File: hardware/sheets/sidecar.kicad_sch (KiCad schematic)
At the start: 6 parts, among them J1 ISA 8-bit (60p)

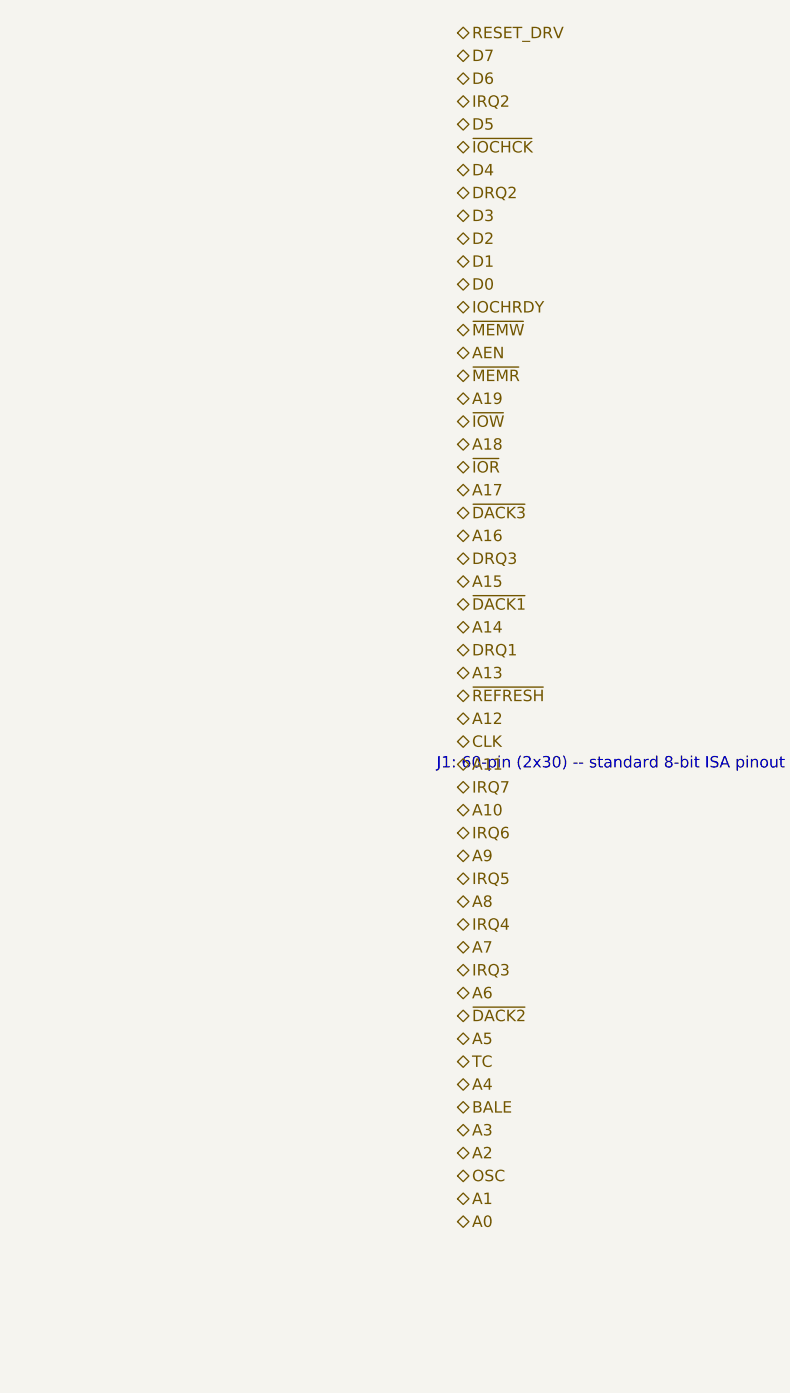
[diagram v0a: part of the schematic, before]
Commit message: ERC cleanup: NC flags on unused pins, anchored interface labels
KiCad 10 ERC drops from 366 to 16 violations, all noise:

- NC flags on the 36 genuinely unused pins (cpu_core '138/'161 spares,
  Supervisor RP2040 unused GPIO, Core2350B GPIO44-47, rtc '138 spares).
- emit_interface anchors every hier label on a stub wire ending in a
  same-name local label -- connectivity unchanged (still by name;
  netlist spans verified), but nothing dangles.
- Interface honesty: cpu_core drops AEN/IOCHRDY from PINS (both live on
  bus_mcu; nothing here touched them), bus_mcu drops PRIV_COUNTER (the
  counter chain is on-sheet, CNT_* never crosses).
- Remaining 6 label_dangling are root IRQ9-13/15: single-sheet by
  design (soft-PIC pull-ups await future 16-bit sources); kept in PINS
  as the AT-style contract.

Co-Authored-By: Claude Fable 5 <noreply@anthropic.com>
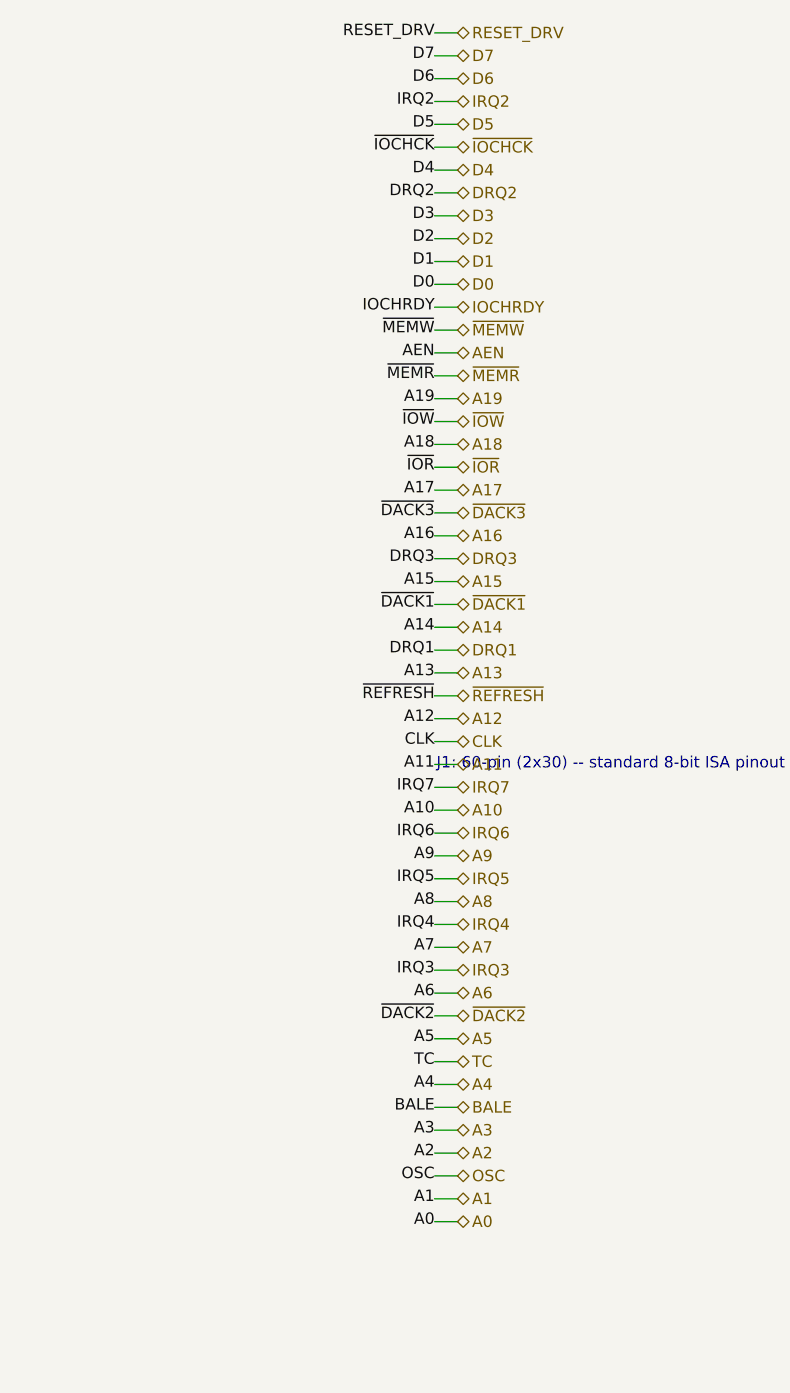
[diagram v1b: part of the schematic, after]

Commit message: Parts: footprints for all components, close 6 LCSC map gaps, check_parts.py
- mxsch.py emits the Footprint property from component props (was
  hard-coded empty); parts.py entries now carry a verified KiCad
  footprint, applied at build time alongside the LCSC number.
- Map keys fixed to match placed values: USB_PROG, SS34, LED (PicoGUS),
  APS6404L, CB3T3257/45 -- every combo across all sheets + cards now
  resolves (130 combos, 455 netlist components, all with footprints).
- Package corrections from JLC DB re-check: RTL8019AS is QFP-100 14x20
  P0.65 (not TQFP); C2897411 female header is a 2x10 strip -- fine for
  Core2350B, Pico needs 2x 1x20 (noted in jlcpcb-sourcing.md).
- 10 mini-xt:* placeholder footprints mark parts whose land pattern is
  authored at layout from the EasyEDA data (CH224K, magnetics, RJ45,
  HDMI, CF socket, ISA slot, switches, Core2350B PGA).
- New tools/check_parts.py: fails on unmapped combos, missing fp
  fields, or footprints absent from the installed KiCad libs.

Co-Authored-By: Claude Fable 5 <noreply@anthropic.com>
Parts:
- C1, C2: footprint (none) -> Capacitor_SMD:C_0603_1608Metric
- C3: footprint (none) -> Capacitor_SMD:C_1206_3216Metric
- D1: footprint (none) -> Diode_SMD:D_SMB
- F1: footprint (none) -> Fuse:Fuse_1812_4532Metric
- J1: footprint (none) -> Connector_PinHeader_2.54mm:PinHeader_2x30_P2.54mm_Vertical
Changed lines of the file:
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@@
 			)
 		)
-		(property "Footprint" ""
+		(property "Footprint" "Connector_PinHeader_2.54mm:PinHeader_2x30_P2.54mm_Vertical"
 			(at 177.8 152.4 0)
 			(effects
@@
 			)
 		)
-		(property "Footprint" ""
+		(property "Footprint" "Fuse:Fuse_1812_4532Metric"
 			(at 203.2 109.22 0)
 			(effects
@@
 			)
 		)
-		(property "Footprint" ""
+		(property "Footprint" "Diode_SMD:D_SMB"
 			(at 218.44 109.22 0)
 			(effects
@@
 			)
 		)
-		(property "Footprint" ""
+		(property "Footprint" "Capacitor_SMD:C_1206_3216Metric"
 			(at 231.14 134.62 0)
 			(effects
@@
 			)
 		)
-		(property "Footprint" ""
+		(property "Footprint" "Capacitor_SMD:C_0603_1608Metric"
 			(at 205.74 134.62 0)
 			(effects
@@
 			)
 		)
-		(property "Footprint" ""
+		(property "Footprint" "Capacitor_SMD:C_0603_1608Metric"
 			(at 218.44 134.62 0)
 			(effects

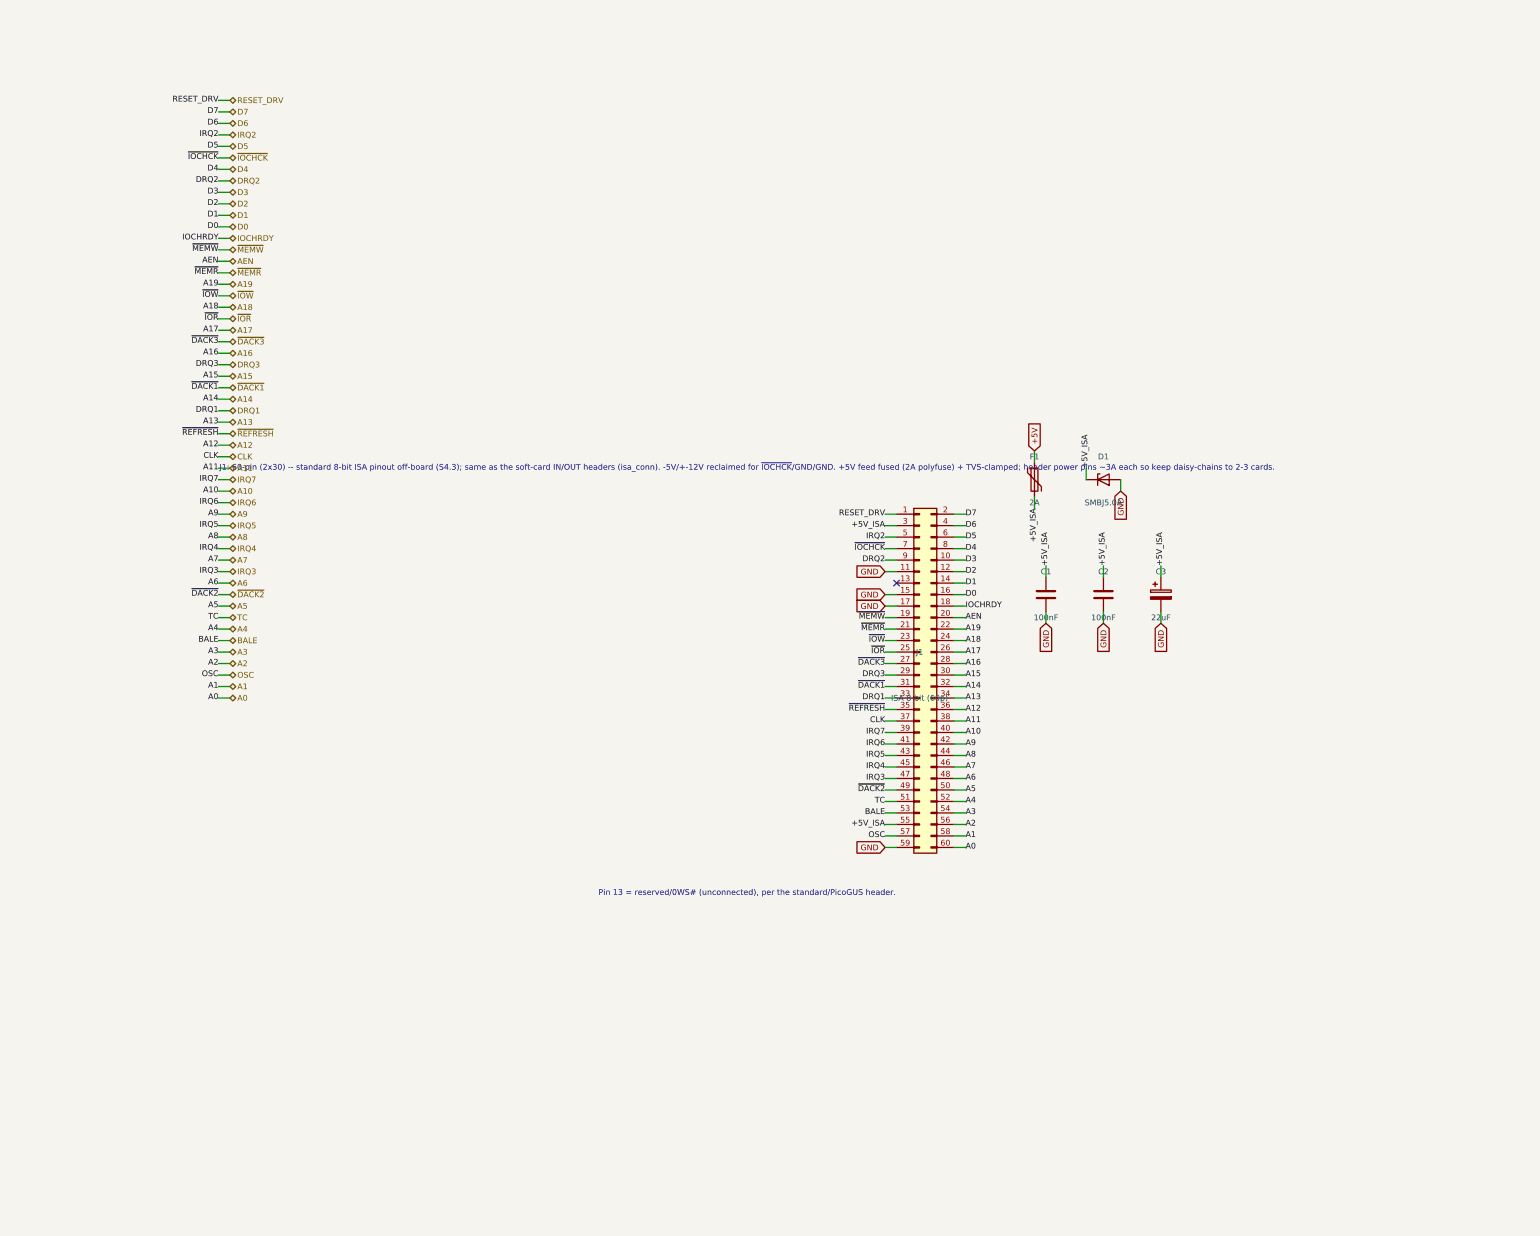
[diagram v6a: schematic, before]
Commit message: sidecar: isolation/buffer bank -- 5V-compatible ISA expansion port
Rewrite the sidecar from a passive 60-pin pass-through into the 3.3V board's
only real-ISA attachment point: an LVC buffer bank (5V-tolerant inputs,
3.3V-TTL outputs) between the internal bus and an external ISA header whose
bus-side nets are port-local (X_*, via isa_conn remap).

- Outbound: 3x 74LVC245A (A0-19 + BALE/AEN/CLK/OSC, DIR strapped outbound) +
  2x 74LVC244A (MEMR/MEMW/IOR/IOW, RESET_DRV, TC, DACK1-3, REFRESH).
- Data: 1x 74LVC245A, DIR = EXP_DDIR, R1 pulls it outbound-safe at power-on
  (DIR=H => A->B; truth table in comment). ~OE tied enabled.
- Inbound: X_IRQ2-7/X_DRQ1-3 -> EXT_* via 2x 74LVC244A, 100k pull-downs on
  every X_ input (unplugged reads all-zeros).
- IOCHRDY/~{IOCHCK}: 74LVC2G07 open-drain (2G06 body + value override) drives
  the internal nets, 10k pull-ups on the X_ side (wired-AND, no contention).
- PINS: filtered copy of isa_conn.ISA_PINS (IRQ/DRQ dropped -> EXT_*), plus
  PRIV_EXP (EXP_DDIR in, EXT_* out); IOCHRDY/~{IOCHCK} kept.

Also refreshes stale build outputs from earlier 3v3 tasks that had edited
sources without rebuilding (network/picogus sheets, card_video net renames),
so committed outputs match current sources. validate_sheet sidecar: zero
structural; build.py exit 0.

Co-Authored-By: Claude Fable 5 <noreply@anthropic.com>
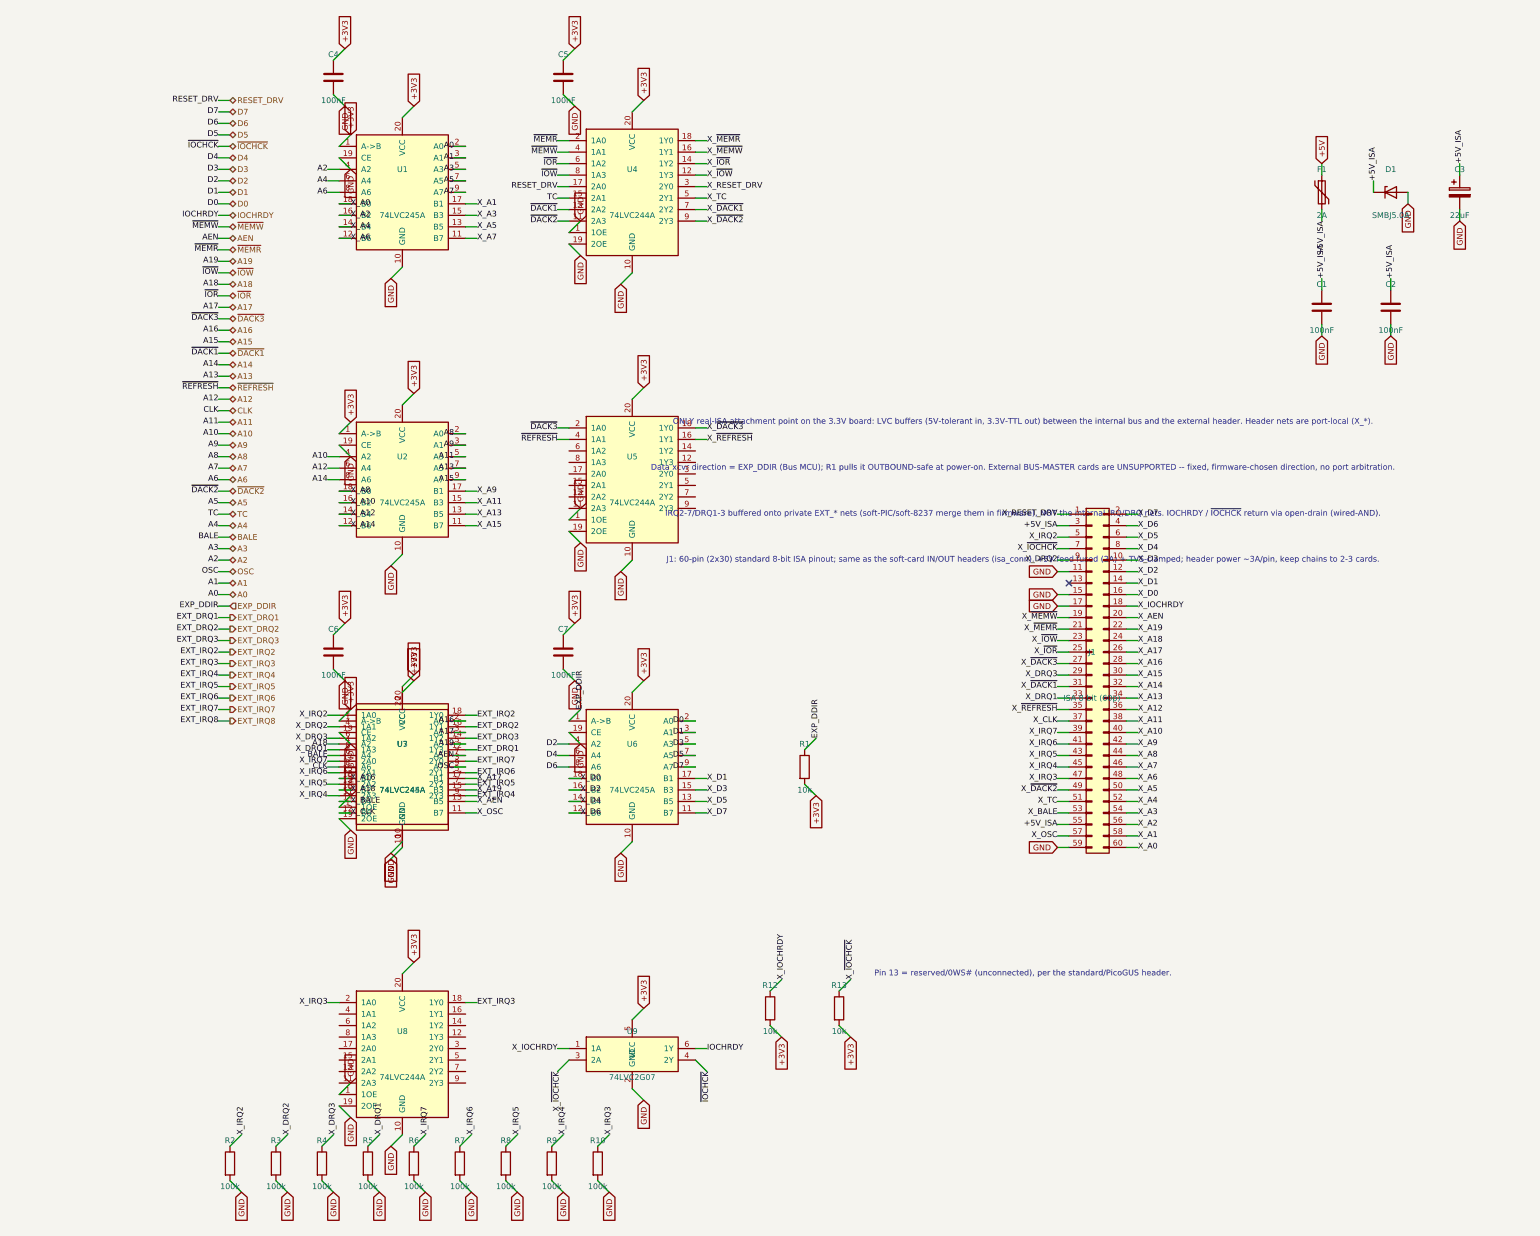
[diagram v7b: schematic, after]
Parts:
- added C4, C5, C6, C7: 100nF, Capacitor_SMD:C_0603_1608Metric, symbol Device:C
- added R1, R12, R13: 10k, Resistor_SMD:R_0603_1608Metric, symbol Device:R
- added R10, R2, R3, R4, R5, R6, R7, R8, R9: 100k, Resistor_SMD:R_0603_1608Metric, symbol Device:R
- added U1, U2, U3, U6: 74LVC245A, Package_SO:TSSOP-20_4.4x6.5mm_P0.65mm, symbol mini-xt:74HCT245
- added U4, U5, U7, U8: 74LVC244A, Package_SO:TSSOP-20_4.4x6.5mm_P0.65mm, symbol mini-xt:74HCT244
- added U9: 74LVC2G07, Package_TO_SOT_SMD:SOT-23-6, symbol mini-xt:74LVC2G06
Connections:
- net A0: now also U1.2 (A0); no longer J1.60 (Pin_60)
- net A1: now also U1.3 (A1); no longer J1.58 (Pin_58)
- net A10: now also U2.4 (A2); no longer J1.40 (Pin_40)
- net A11: now also U2.5 (A3); no longer J1.38 (Pin_38)
- net A12: now also U2.6 (A4); no longer J1.36 (Pin_36)
- net A13: now also U2.7 (A5); no longer J1.34 (Pin_34)
- net A14: now also U2.8 (A6); no longer J1.32 (Pin_32)
- net A15: now also U2.9 (A7); no longer J1.30 (Pin_30)
- net A16: now also U3.2 (A0); no longer J1.28 (Pin_28)
- net A17: now also U3.3 (A1); no longer J1.26 (Pin_26)
- net A18: now also U3.4 (A2); no longer J1.24 (Pin_24)
- net A19: now also U3.5 (A3); no longer J1.22 (Pin_22)
- net A2: now also U1.4 (A2); no longer J1.56 (Pin_56)
- net A3: now also U1.5 (A3); no longer J1.54 (Pin_54)
- net A4: now also U1.6 (A4); no longer J1.52 (Pin_52)
- net A5: now also U1.7 (A5); no longer J1.50 (Pin_50)
- net A6: now also U1.8 (A6); no longer J1.48 (Pin_48)
- net A7: now also U1.9 (A7); no longer J1.46 (Pin_46)
- net A8: now also U2.2 (A0); no longer J1.44 (Pin_44)
- net A9: now also U2.3 (A1); no longer J1.42 (Pin_42)
- net AEN: now also U3.7 (A5); no longer J1.20 (Pin_20)
- net BALE: now also U3.6 (A4); no longer J1.53 (Pin_53)
- net CLK: now also U3.8 (A6); no longer J1.37 (Pin_37)
- net D0: now also U6.2 (A0); no longer J1.16 (Pin_16)
- net D1: now also U6.3 (A1); no longer J1.14 (Pin_14)
- net D2: now also U6.4 (A2); no longer J1.12 (Pin_12)
- net D3: now also U6.5 (A3); no longer J1.10 (Pin_10)
- net D4: now also U6.6 (A4); no longer J1.8 (Pin_8)
- net D5: now also U6.7 (A5); no longer J1.6 (Pin_6)
- net D6: now also U6.8 (A6); no longer J1.4 (Pin_4)
- net D7: now also U6.9 (A7); no longer J1.2 (Pin_2)
- net GND: now also C4.2, C5.2, C6.2, C7.2, R10.2, R2.2, R3.2, R4.2, R5.2, R6.2, R7.2, R8.2, R9.2, U1.10 (GND), U1.19 (CE), U2.10 (GND), U2.19 (CE), U3.10 (GND), U3.19 (CE), U4.1 (1OE), U4.10 (GND), U4.19 (2OE), U5.1 (1OE), U5.10 (GND), U5.19 (2OE), U6.10 (GND), U6.19 (CE), U7.1 (1OE), U7.10 (GND), U7.19 (2OE), U8.1 (1OE), U8.10 (GND), U8.19 (2OE), U9.2 (GND)
- net IOCHRDY: now also U9.6 (1Y); no longer J1.18 (Pin_18)
- net OSC: now also U3.9 (A7); no longer J1.57 (Pin_57)
- net RESET_DRV: now also U4.17 (2A0); no longer J1.1 (Pin_1)
- net TC: now also U4.15 (2A1); no longer J1.51 (Pin_51)
- net ~{DACK1}: now also U4.13 (2A2); no longer J1.31 (Pin_31)
- net ~{DACK2}: now also U4.11 (2A3); no longer J1.49 (Pin_49)
- net ~{DACK3}: now also U5.2 (1A0); no longer J1.27 (Pin_27)
- net ~{IOCHCK}: now also U9.4 (2Y); no longer J1.7 (Pin_7)
- net ~{IOR}: now also U4.6 (1A2); no longer J1.25 (Pin_25)
- net ~{IOW}: now also U4.8 (1A3); no longer J1.23 (Pin_23)
- net ~{MEMR}: now also U4.2 (1A0); no longer J1.21 (Pin_21)
- net ~{MEMW}: now also U4.4 (1A1); no longer J1.19 (Pin_19)
- net ~{REFRESH}: now also U5.4 (1A1); no longer J1.35 (Pin_35)
- net DRQ1 renamed X_DRQ1
- net X_DRQ1: now also R5.1, U7.8 (1A3)
- net DRQ2 renamed X_DRQ2
- net X_DRQ2: now also R3.1, U7.4 (1A1)
- net DRQ3 renamed X_DRQ3
- net X_DRQ3: now also R4.1, U7.6 (1A2)
- net IRQ2 renamed X_IRQ2
- net X_IRQ2: now also R2.1, U7.2 (1A0)
- net IRQ3 renamed X_IRQ3
- net X_IRQ3: now also R10.1, U8.2 (1A0)
- net IRQ4 renamed X_IRQ4
- net X_IRQ4: now also R9.1, U7.11 (2A3)
- net IRQ5 renamed X_IRQ5
- net X_IRQ5: now also R8.1, U7.13 (2A2)
- net IRQ6 renamed X_IRQ6
- net X_IRQ6: now also R7.1, U7.15 (2A1)
- net IRQ7 renamed X_IRQ7
- net X_IRQ7: now also R6.1, U7.17 (2A0)
- new net +3V3: C4.1, C5.1, C6.1, C7.1, R1.2, R12.2, R13.2, U1.1 (A->B), U1.20 (VCC), U2.1 (A->B), U2.20 (VCC), U3.1 (A->B), U3.20 (VCC), U4.20 (VCC), U5.20 (VCC), U6.20 (VCC), U7.20 (VCC), U8.20 (VCC), U9.5 (VCC)
- new net EXP_DDIR: R1.1, U6.1 (A->B)
- new net EXT_DRQ1: U7.12 (1Y3)
- new net EXT_DRQ2: U7.16 (1Y1)
- new net EXT_DRQ3: U7.14 (1Y2)
- new net EXT_IRQ2: U7.18 (1Y0)
- new net EXT_IRQ3: U8.18 (1Y0)
- new net EXT_IRQ4: U7.9 (2Y3)
- new net EXT_IRQ5: U7.7 (2Y2)
- new net EXT_IRQ6: U7.5 (2Y1)
- new net EXT_IRQ7: U7.3 (2Y0)
- new net X_A0: J1.60 (Pin_60), U1.18 (B0)
- new net X_A1: J1.58 (Pin_58), U1.17 (B1)
- new net X_A10: J1.40 (Pin_40), U2.16 (B2)
- new net X_A11: J1.38 (Pin_38), U2.15 (B3)
- new net X_A12: J1.36 (Pin_36), U2.14 (B4)
- new net X_A13: J1.34 (Pin_34), U2.13 (B5)
- new net X_A14: J1.32 (Pin_32), U2.12 (B6)
- new net X_A15: J1.30 (Pin_30), U2.11 (B7)
- new net X_A16: J1.28 (Pin_28), U3.18 (B0)
- new net X_A17: J1.26 (Pin_26), U3.17 (B1)
- new net X_A18: J1.24 (Pin_24), U3.16 (B2)
- new net X_A19: J1.22 (Pin_22), U3.15 (B3)
- new net X_A2: J1.56 (Pin_56), U1.16 (B2)
- new net X_A3: J1.54 (Pin_54), U1.15 (B3)
- new net X_A4: J1.52 (Pin_52), U1.14 (B4)
- new net X_A5: J1.50 (Pin_50), U1.13 (B5)
- new net X_A6: J1.48 (Pin_48), U1.12 (B6)
- new net X_A7: J1.46 (Pin_46), U1.11 (B7)
- new net X_A8: J1.44 (Pin_44), U2.18 (B0)
- new net X_A9: J1.42 (Pin_42), U2.17 (B1)
- new net X_AEN: J1.20 (Pin_20), U3.13 (B5)
- new net X_BALE: J1.53 (Pin_53), U3.14 (B4)
- new net X_CLK: J1.37 (Pin_37), U3.12 (B6)
- new net X_D0: J1.16 (Pin_16), U6.18 (B0)
- new net X_D1: J1.14 (Pin_14), U6.17 (B1)
- new net X_D2: J1.12 (Pin_12), U6.16 (B2)
- new net X_D3: J1.10 (Pin_10), U6.15 (B3)
- new net X_D4: J1.8 (Pin_8), U6.14 (B4)
- new net X_D5: J1.6 (Pin_6), U6.13 (B5)
- new net X_D6: J1.4 (Pin_4), U6.12 (B6)
- new net X_D7: J1.2 (Pin_2), U6.11 (B7)
- new net X_IOCHRDY: J1.18 (Pin_18), R12.1, U9.1 (1A)
- new net X_OSC: J1.57 (Pin_57), U3.11 (B7)
- new net X_RESET_DRV: J1.1 (Pin_1), U4.3 (2Y0)
- new net X_TC: J1.51 (Pin_51), U4.5 (2Y1)
- new net X_~{DACK1}: J1.31 (Pin_31), U4.7 (2Y2)
- new net X_~{DACK2}: J1.49 (Pin_49), U4.9 (2Y3)
- new net X_~{DACK3}: J1.27 (Pin_27), U5.18 (1Y0)
- new net X_~{IOCHCK}: J1.7 (Pin_7), R13.1, U9.3 (2A)
- new net X_~{IOR}: J1.25 (Pin_25), U4.14 (1Y2)
- new net X_~{IOW}: J1.23 (Pin_23), U4.12 (1Y3)
- new net X_~{MEMR}: J1.21 (Pin_21), U4.18 (1Y0)
- new net X_~{MEMW}: J1.19 (Pin_19), U4.16 (1Y1)
- new net X_~{REFRESH}: J1.35 (Pin_35), U5.16 (1Y1)
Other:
- note added: "Data xcvr direction = EXP_DDIR (Bus MCU); R1 pulls it OUTBOUND-safe at power-on. External BUS-MASTER cards are UNSUPPORTED -- fixed, firmware-chosen direction, no port arbitration."
- note added: "IRQ2-7/DRQ1-3 buffered onto private EXT_* nets (soft-PIC/soft-8237 merge them in firmware), NOT the internal IRQ/DRQ nets. IOCHRDY / ~{IOCHCK} return via open-drain (wired-AND)."
- note added: "J1: 60-pin (2x30) standard 8-bit ISA pinout; same as the soft-card IN/OUT headers (isa_conn). +5V feed fused (2A) + TVS-clamped; header power ~3A/pin, keep chains to 2-3 cards."
- note added: "ONLY real-ISA attachment point on the 3.3V board: LVC buffers (5V-tolerant in, 3.3V-TTL out) between the internal bus and the external header. Header nets are port-local (X_*)."
- note removed: "J1: 60-pin (2x30) -- standard 8-bit ISA pinout off-board (S4.3); same as the soft-card IN/OUT headers (isa_conn). -5V/+-12V reclaimed for ~{IOCHCK}/GND/GND. +5V feed fused (2A polyfuse) + TVS-clamped; header power pins ~3A each so keep daisy-chains to 2-3 cards."
- title: Sidecar -- 60-pin (2x30) ISA expansion header -> Sidecar -- buffered 5V-compatible ISA expansion port
